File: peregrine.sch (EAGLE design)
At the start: 42 parts, among them J1 AVR_SPI_PRG_6PTH, Q1 8MHz, U1 ITG-3200, U2 ADXL345, U5 3.3V, U6 ATMEGA328

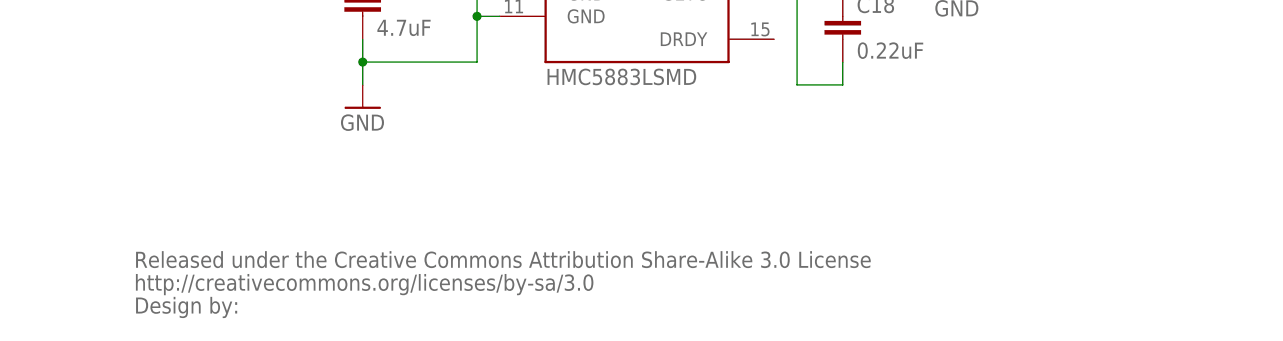
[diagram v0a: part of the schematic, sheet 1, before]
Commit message: Added schematics, TODO, fixed gitignore
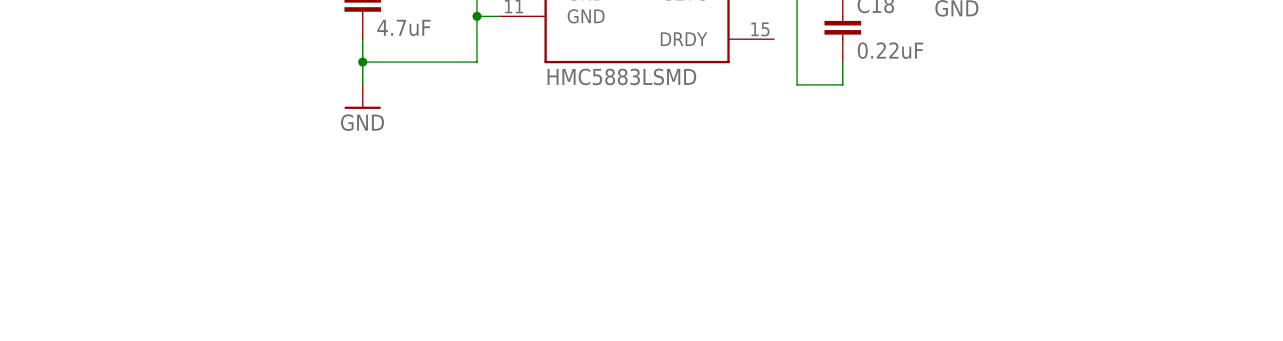
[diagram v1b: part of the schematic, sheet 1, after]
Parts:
- removed U$2, U$3: CREATIVE_COMMONS, SparkFun:CREATIVE_COMMONS
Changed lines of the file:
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@@
 <part name="U2" library="SparkFun" deviceset="ADXL345" device=""/>
 <part name="U$1" library="SparkFun" deviceset="HMC5883L" device="SMD"/>
-<part name="U$2" library="SparkFun" deviceset="CREATIVE_COMMONS" device=""/>
 <part name="U$4" library="SparkFun" deviceset="OSHW-LOGO" device="L"/>
 <part name="C22" library="SparkFun" deviceset="CAP" device="0402-CAP" value="0.1uF"/>
@@
 <part name="GND10" library="SparkFun" deviceset="GND" device=""/>
 <part name="JP10" library="SparkFun" deviceset="M02" device="PTH" value="JST_Horizontal"/>
-<part name="U$3" library="SparkFun" deviceset="CREATIVE_COMMONS" device=""/>
 <part name="JP11" library="abes" deviceset="FIDUCIAL" device="1X2.5"/>
 <part name="JP12" library="abes" deviceset="FIDUCIAL" device="1X2.5"/>
@@
 <instance part="U2" gate="G$1" x="76.2" y="134.62"/>
 <instance part="U$1" gate="G$1" x="68.58" y="53.34"/>
-<instance part="U$2" gate="G$1" x="12.7" y="10.16"/>
 <instance part="U$4" gate="G$1" x="210.82" y="33.02"/>
 </instances>
@@
 <instance part="GND10" gate="1" x="88.9" y="137.16"/>
 <instance part="JP10" gate="G$1" x="22.86" y="73.66"/>
-<instance part="U$3" gate="G$1" x="15.24" y="12.7"/>
 <instance part="JP11" gate="G$1" x="152.4" y="30.48"/>
 <instance part="JP12" gate="G$1" x="154.94" y="30.48"/>

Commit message: Re-arranged Schematic, updated uC to ATMEGA32U4
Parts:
- removed C13, C22, C29: 0.1uF, SparkFun:CAP0402-CAP
- removed C18: 0.22uF, SparkFun:CAP0402-CAP
- removed D3: Green, SparkFun:LED0603
- removed JP10: JST_Horizontal, SparkFun:M02PTH
- removed JP11, JP12: FIDUCIAL1X2.5, abes:FIDUCIAL1X2.5
- removed JP5, JP6: STAND-OFF, SparkFun:STAND-OFF
- removed Q1: 8MHz, SparkFun:RESONATORSMD
- removed R10, R11: 10K, SparkFun:RESISTOR0402-RES
- removed R12: 330, SparkFun:RESISTOR0402-RES
- removed S1: Reset, SparkFun:SWITCH-MOMENTARY-2SMD
- removed S2: Power, SparkFun:SWITCH-DPDTSMD
- removed U$1: HMC5883LSMD, SparkFun:HMC5883LSMD
- removed U$4: OSHW-LOGOL, SparkFun:OSHW-LOGOL
- removed U6: ATMEGA328, SparkFun:ATMEGA168
- added C10, C5, C7, C9: 0.1uF, SparkFun:CAP0402-CAP
- added C11, C12: 4.7uF, SparkFun:CAP0402-CAP
- added C28: 100n, SmartPrj:C-EUC0603
- added C31, C32: 22p, SmartPrj:C-EUC0603
- added C4: 0.22uF, SparkFun:CAP0402-CAP
- added C6: 2.2nF, SparkFun:CAP0402-CAP
- added C8: 10nF, SparkFun:CAP0402-CAP
- added D2: CD1206-S01575, diode:DIODE-MINIMELF
- added F1: MF-MSMF050-2 500mA, rcl:L-EUL1812
- added GPS: EM408_CON, SparkFun:EM408_CON
- added IC2: LMV358IDGKR, linear:LMV358MMX
- added ICSP: ICSP, SmartPrj:PINHD-2X3
- added JP8, JP9: (no value), SparkFun:M03PTH
- added L, RX, TX: Yellow, led:LEDCHIPLED_0805
- added L1, L2: MH2029-300Y, wuerth-elektronik:WE-CBF_0805
- added ON: Green, led:LEDCHIPLED_0805
- added R3: 330, SparkFun:RESISTOR0402-RES
- added R5: 1M, SmartPrj:R-EU_R0603
- added R6, R7: NM, SmartPrj:R-EU_R0402
- added REC: (no value), SparkFun:M06SIP
- added REC_POWER: (no value), SparkFun:M02PTH
- added RESET: TS42, SmartPrj:TS42
- added RN1: 10K, resistor-dil:4R-NCAY16
- added RN2: 1K, resistor-dil:4R-NCAY16
- added RN3: 22R, resistor-dil:4R-NCAY16
- added U$2: HMC5883LSMD, SparkFun:HMC5883LSMD
- added U4: 3.3V, SparkFun:V_REG_LDOSMD
- added Y1: 16MHz KX-7, SmartPrj:CRYSTAL-3.2-2.5
- added Z1, Z2: CG0603MLC-05E, varistor:VARISTORCN0603
- C2: value 2.2nF -> 0.1uF
- C21: value 4.7uF -> 100n; device SparkFun:CAP0402-CAP -> SmartPrj:C-EUC0603
- C23: value 10uF -> 1uF; device SparkFun:CAP_POL1206 -> SmartPrj:C-EUC0603
- C24: value 0.1uF -> 1uF; device SparkFun:CAP0402-CAP -> SmartPrj:C-EUC0603
- C25: value 0.1uF -> 100n; device SparkFun:CAP0402-CAP -> SmartPrj:C-EUC0603
- C26: value 10uF -> 100n; device SparkFun:CAP_POL1206 -> SmartPrj:C-EUC0603
- C27: value 0.1uF -> 10u; device SparkFun:CAP0402-CAP -> rcl:CPOL-EUSMCB
- C3: value 10nF -> 4.7uF
- J1: value AVR_SPI_PRG_6PTH -> USB MICRO; device SparkFun:AVR_SPI_PRG_6PTH -> SmartPrj:MYCON2_USB-MINI-B
- JP1: value JST_Horizontal -> (none); device SparkFun:M02-JST-2MM-SMT -> SparkFun:M03PTH
- JP2, JP4: value STAND-OFF -> (none); device SparkFun:STAND-OFF -> SparkFun:M03PTH
- JP3: value LOGO-SFENEW -> (none); device SparkFun:LOGO-SFENEW -> SparkFun:M04PTH
- JP7: value FTDI Basic -> (none); device SparkFun:ARDUINO_SERIAL_PROGRAMPTH -> SparkFun:M03PTH
- LED1: value Red -> Blue
- R1: value 4.7k -> 4.7K
- U5: value 3.3V -> ATMEGA32U4-XUAU; device SparkFun:V_REG_LDOSMD -> SmartPrj:ATMEGA32U4-XUAU
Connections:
- removed net 3.3V: C13.1, C22.1, C23.+, C24.2, C29.1, C3.1, J1.2, JP7.VCC, R1.2, R10.2, R11.2, R2.2, U$1.S1, U$1.VDD, U$1.VDDIO, U1.VDD, U1.VLOGIC, U2.CS, U2.VDD, U2.VSS, U5.OUT, U6.AVCC, U6.VCC@1, U6.VCC@2
- removed net DTR: C27.2, JP7.DTR
- removed net N$13: Q1.1, U6.PB7(XTAL2/TOSC2)
- removed net N$14: Q1.3, U6.PB6(XTAL1/TOSC1)
- removed net N$15: JP1.2, JP10.2, S2.2, S2.5
- removed net N$38: LED1.A, R11.1
- removed net N$6: C21.1, U$1.C1
- removed net RAW: C26.+, S2.1, S2.4, U5.EN, U5.IN
- removed net RXI: JP7.TXO, U6.PD0(RXD)
- removed net TXO: JP7.RXI, U6.PD1(TXD)
- new net +5V: C25.1, C26.1, D2.C, ICSP.2, JP1.2, JP2.2, JP4.2, JP7.2, JP8.2, JP9.2, L1.1, REC_POWER.2, RN1D.2, RN2A.1, RN2C.1, RN2D.1, U5.UVCC, U5.VCC, U5.VCC1
- new net 3V3: C1.1, C10.1, C12.1, C2.1, C5.1, C8.1, C9.1, GPS.EN, GPS.VCC, LED1.A, R1.2, R2.2, U$2.S1, U$2.VDD, U$2.VDDIO, U1.VDD, U1.VLOGIC, U2.CS, U2.VDD, U2.VSS, U4.OUT
- new net A0: U5.(ADC7/TDI)PF7
- new net A1: U5.(ADC6/TDO)PF6
- new net A2: U5.(ADC5/TMS)PF5
- new net A3: U5.(ADC4/TCK)PF4
- new net A4: U5.(ADC1)PF1
- new net A5: U5.(ADC0)PF0
- new net AGND: C21.1, R6.1, U5.GND3
- new net AVCC: C24.1, L1.2, U5.AVCC, U5.AVCC1
- new net COM: GPS.GND, REC_POWER.1
- new net D+: J1.D+, RN3A.2, Z1.1
- new net D-: J1.D-, RN3D.2, Z2.1
- new net D0/RX: U5.(RXD1/AIN1/INT2)PD2
- new net D1/TX: U5.(TXD1/INT3)PD3
- new net D2/SDA: U5.(SDA/INT1)PD1
- new net D3/SCL: U5.(OC0B/SCL/INT0)PD0
- new net D4: U5.(ICP1/ADC8)PD4
- new net D5*: U5.(OC3A/#0C4A)PC6
- new net D6*: U5.(T0/OC4D/ADC10)PD7
- new net D7: U5.(INT6/AIN0)PE6
- new net GPS-RX: GPS.TX
- new net GPS-TX: GPS.RX
- new net HWB: RN1C.2, U5.(#HWB)PE2
- new net IO10*: U5.(PCINT6/OC1B/OC4B/ADC13)PB6
- new net IO11*: U5.(PCINT7/OC0A/OC1C/#RTS)PB7
- new net IO12: U5.(T1/#OC4D/ADC9)PD6
- new net IO13*: IC2A.+IN, U5.(ICP3/CLK0/OC4A)PC7
- new net IO8: U5.(ADC11/PCINT4)PB4
- new net IO9*: U5.(PCINT5/OC1A/#OC4B/ADC12)PB5
- new net LL: IC2A.-IN, IC2A.OUT, RN2B.1
- new net M_1: JP1.3
- new net M_2: JP2.3
- new net M_3: JP4.3
- new net M_4: JP7.3
- new net M_AUX1: JP9.3
- new net M_AUX2: JP8.3
- new net N$11: RN2C.2, TX.A
- new net N$5: C6.1, U1.CPOUT
- new net N$7: C7.1, U1.REGOUT
- new net N$8: ON.A, RN2A.2
- new net N$9: L.A, RN2B.2
- new net RD+: RN3A.1, U5.D+
- new net RD-: RN3D.1, U5.D-
- new net REC1: REC.1
- new net REC2: REC.2
- new net REC3: REC.3
- new net REC4: REC.4
- new net REC5: REC.5
- new net REC6: REC.6
- new net RXLED: RX.C, U5.(SS/PCINT0)PB0
- new net TXLED: TX.C, U5.(XCK1/#CTS)PD5
- new net UCAP: C23.1, U5.UCAP
- new net UGND: C23.2, J1.GND, L2.1, R7.2, U5.UGND
- new net USBID: J1.ID
- new net VCC: C11.1, JP3.4, U4.EN, U4.IN
- new net VUSB: C27.+, C28.2, F1.1, U5.VBUS
- new net XTAL1: C32.1, R5.1, U5.XTAL1, Y1.C1
- new net XTAL2: C31.2, R5.2, U5.XTAL2, Y1.C2
- new net XUSB: F1.2, J1.VBUS
- net AREF: now also C21.2, U5.AREF; no longer C25.2, U6.AREF
- net GND: now also C10.2, C11.2, C12.2, C24.2, C25.2, C26.2, C27.-, C28.1, C31.1, C32.2, C5.2, C6.2, C7.2, C8.2, C9.2, ICSP.6, J1.SH1, J1.SH2, J1.SH3, J1.SH4, J1.SH5, J1.SH6, JP2.1, JP3.3, JP4.1, JP7.1, JP8.1, JP9.1, L.C, L2.2, ON.C, R3.1, R6.2, R7.1, RESET.3, RESET.4, RN1C.1, U$2.GND@1, U$2.GND@2, U4.GND, U5.GND1, U5.GND2, U5.PAD, Y1.GND@1, Y1.GND@2, Z1.2, Z2.2; no longer C13.2, C21.2, C22.2, C23.-, C24.1, C25.1, C26.-, C29.2, D3.C, J1.6, JP10.1, JP7.CTS, JP7.GND, LED1.C, Q1.2, S1.1, U$1.GND@1, U$1.GND@2, U6.AGND, U6.GND@1, U6.GND@2
- net MISO: now also ICSP.1, U5.(PD0/MISO/PCINT3)PB3; no longer J1.1, U6.PB4(MISO)
- net MOSI: now also ICSP.4, U5.(PDI/MOSI/PCINT2)PB2; no longer J1.4, U6.PB3(MOSI/OC2)
- net N$1: now also C3.1, U$2.C1; no longer C18.2, U$1.SETP
- net N$12: now also RN2D.2, RX.A; no longer D3.A, R12.2
- net N$2: now also C4.1, U$2.SETP; no longer C18.1, U$1.SETC
- net N$3: now also C4.2, U$2.SETC; no longer C1.1, U1.REGOUT
- net N$4: now also LED1.C, R3.2; no longer C2.1, U1.CPOUT
- net RESET: now also D2.A, ICSP.5, RESET.1, RESET.2, RN1D.1, U5.RESET; no longer C27.1, J1.5, R10.1, S1.2, U6.PC6(/RESET)
- net SCK: now also ICSP.3, U5.(SCLK/PCINT1)PB1; no longer J1.3, R12.1, U6.PB5(SCK)
- net SCL: now also JP3.1, U$2.SCL; no longer U$1.SCL, U6.PC5(ADC5/SCL)
- net SDA: now also JP3.2, U$2.SDA; no longer U$1.SDA, U6.PC4(ADC4/SDA)
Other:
- note added: "Accel"
- note added: "Compass"
- note added: "Gyro"
- note added: "Level Conversion / Indication"
- note added: "Microcontroller"
- note added: "Pins 'n Stuff"
- note added: "Power"
- note added: "Pressure"
- note added: "Sensors"
- note added: "USB"
- note added: "USB boot En"
- note removed: "-------------------------"
- note removed: "0xA6 for write, 0xA7 for read"
- note removed: "0xD0 for write, 0xD1 for read"
- note removed: "ACCEL"
- note removed: "AVR"
- note removed: "AVR SPI"
- note removed: "Barometer"
- note removed: "GYRO"
- note removed: "INTERFACE"
- note removed: "MAG"
- note removed: "Max Current Output: 150mA"
- note removed: "Max Voltage Input: 16VDC"
- note removed: "POWER"

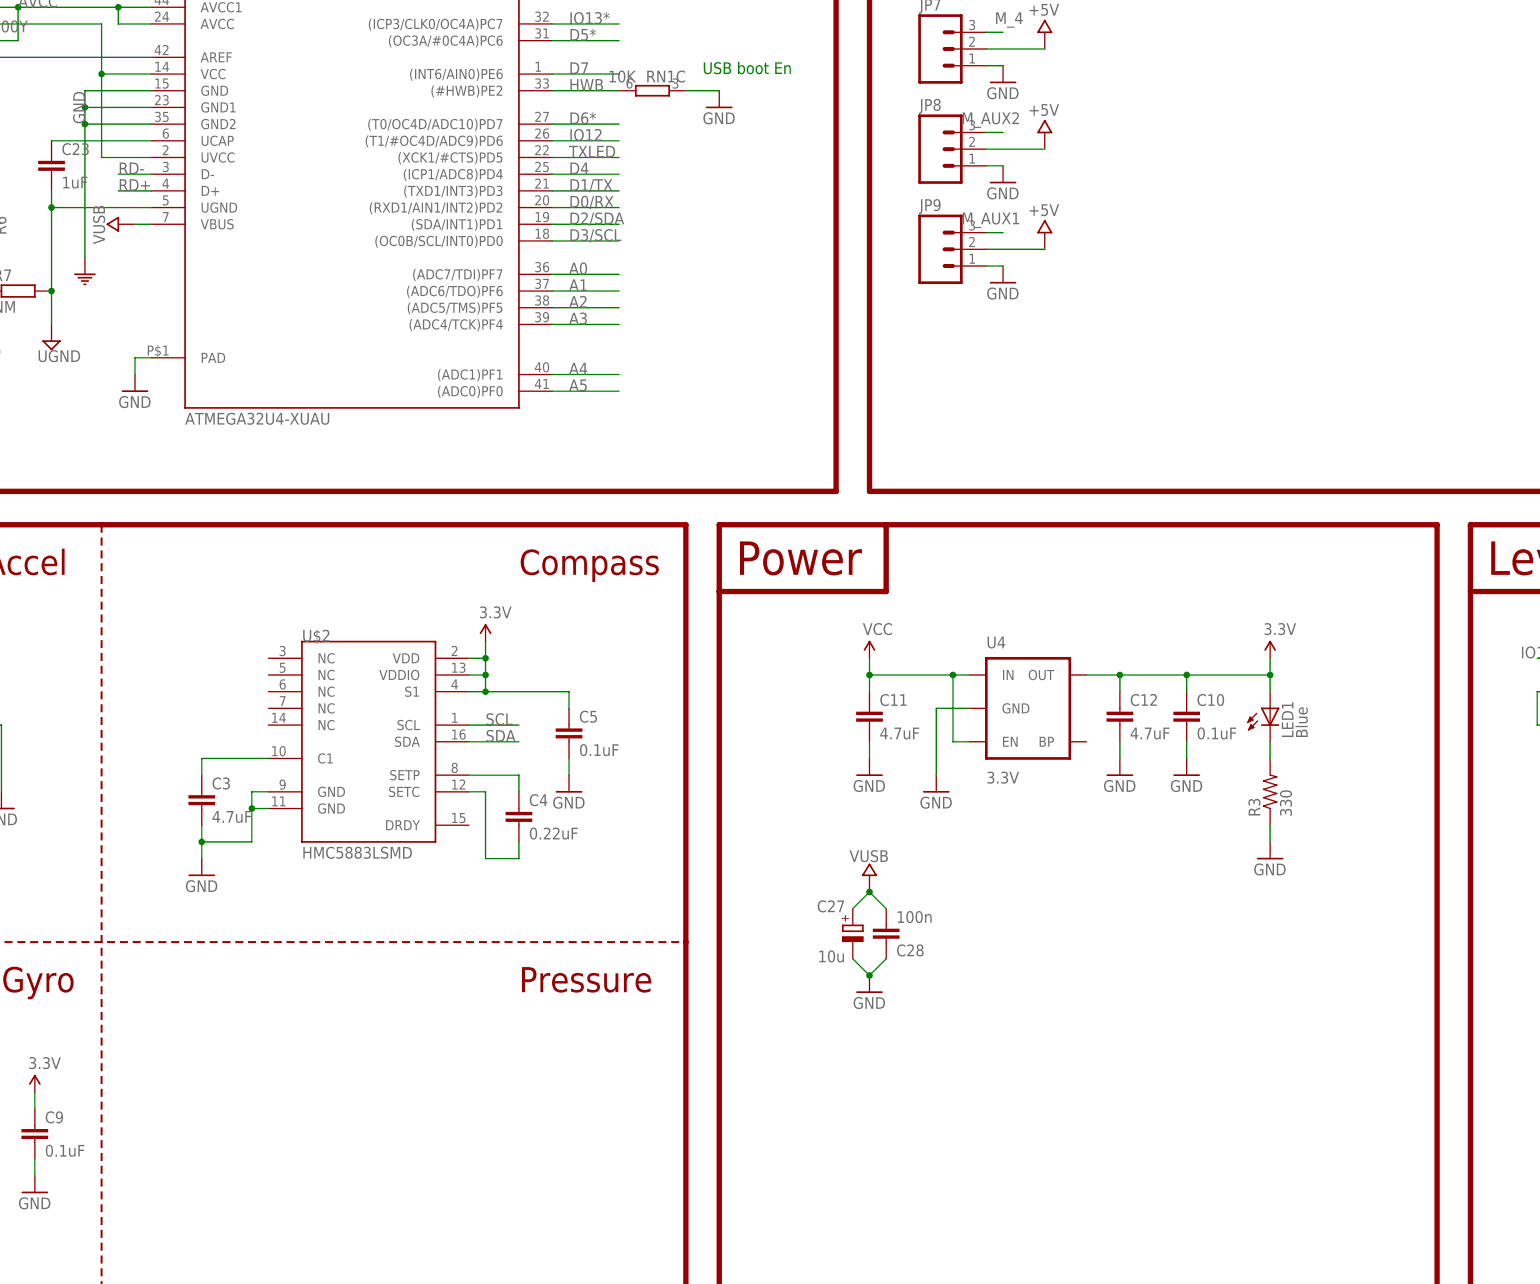
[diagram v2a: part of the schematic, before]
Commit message: Added barometers, JTAG, datasheets
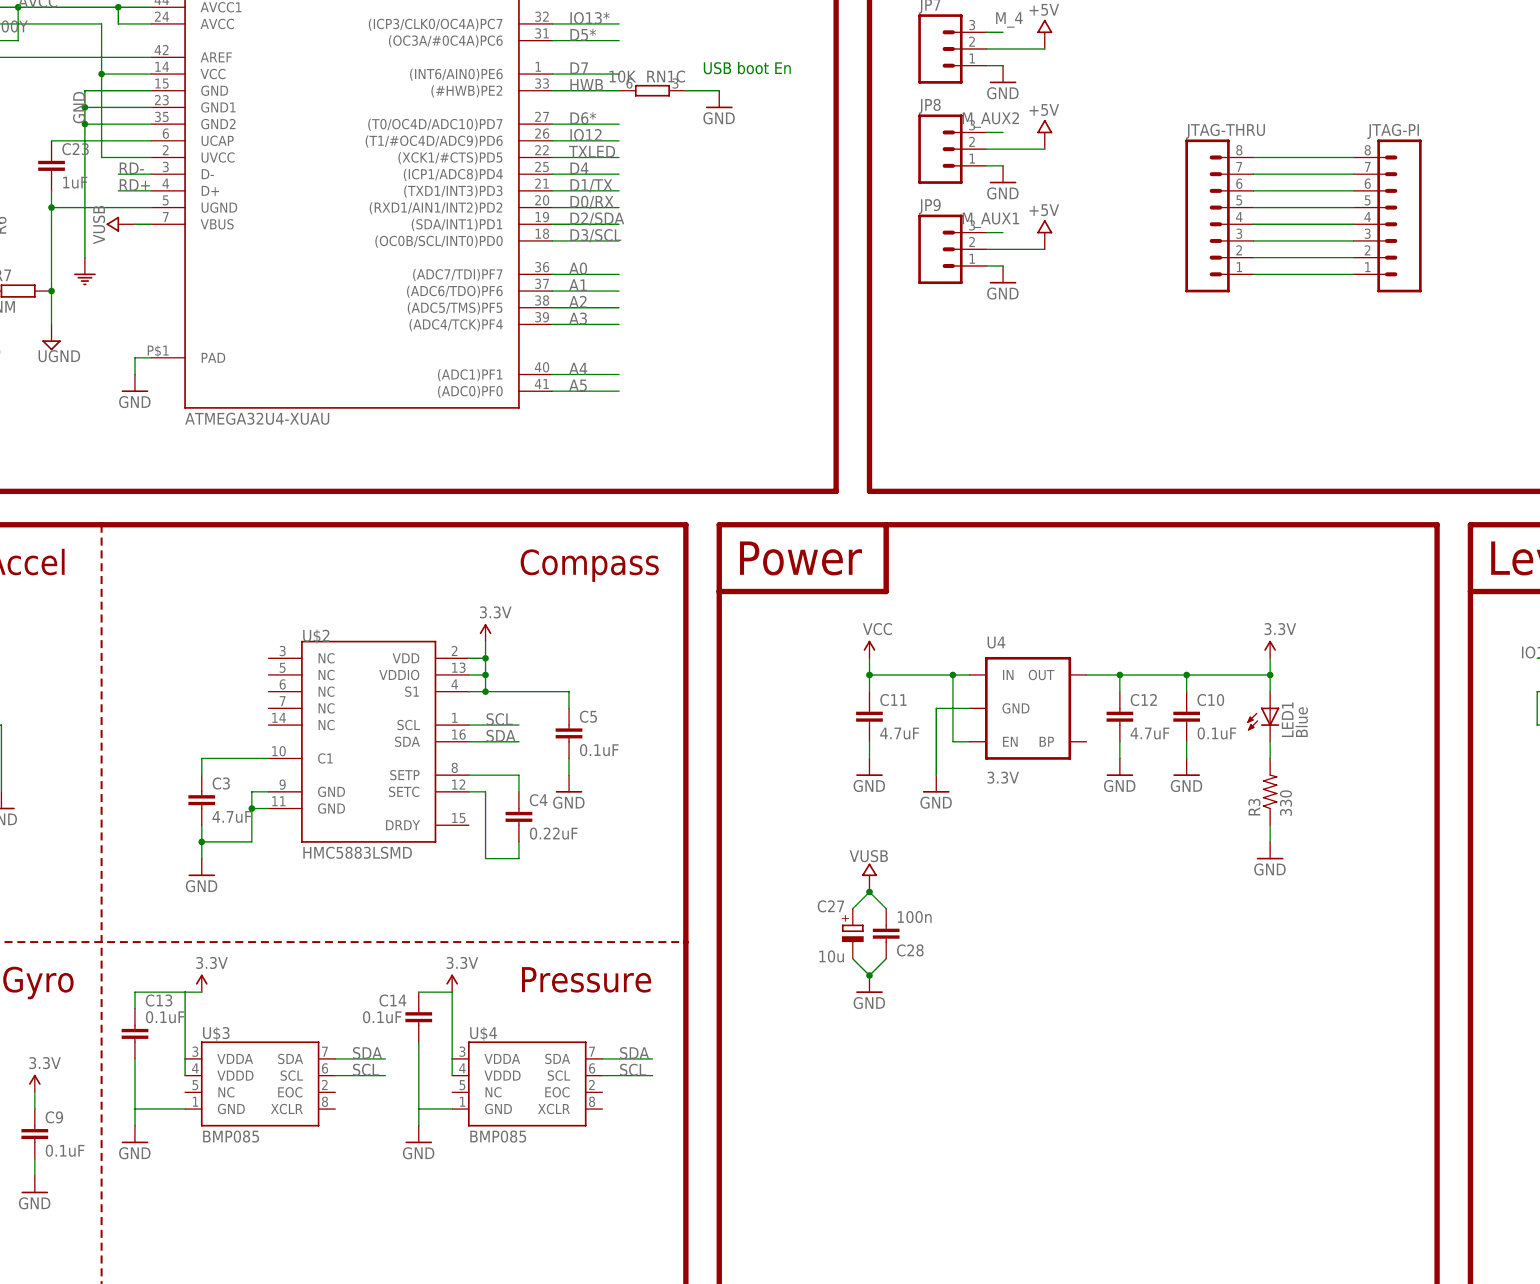
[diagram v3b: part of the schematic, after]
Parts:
- added C13, C14: 0.1uF, SparkFun:CAP0402-CAP
- added JTAG-PI: (no value), SparkFun:M083.5MM-8
- added JTAG-THRU: (no value), SparkFun:M081X08
- added U$3, U$4: BMP085, SparkFun:BMP085
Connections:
- new net 3.3V: C13.1, C14.1, U$3.VDDA, U$3.VDDD, U$4.VDDA, U$4.VDDD
- new net N$10: U$3.SDA
- new net N$13: U$3.SCL
- new net N$14: JTAG-PI.7, JTAG-THRU.7
- new net N$15: U$4.SDA
- new net N$16: U$4.SCL
- new net N$17: JTAG-PI.6, JTAG-THRU.6
- new net N$18: JTAG-PI.5, JTAG-THRU.5
- new net N$19: JTAG-PI.4, JTAG-THRU.4
- new net N$20: JTAG-PI.3, JTAG-THRU.3
- new net N$21: JTAG-PI.2, JTAG-THRU.2
- new net N$22: JTAG-PI.1, JTAG-THRU.1
- new net N$6: JTAG-PI.8, JTAG-THRU.8
- net GND: now also C13.2, C14.2, U$3.GND, U$4.GND
